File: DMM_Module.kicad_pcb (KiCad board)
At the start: 2 copper layers, 60 x 96 mm, 11 parts, among them J1 M20-7810245, J2 M20-7810245, J3 M20-7810245, J4 M20-7810245, J5 M20-7812045, J6 M20-7812045

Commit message: preliminary placement
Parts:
- added C1: 5p, Capacitor_SMD:C_0603_1608Metric, F.Cu at (74.3, 97.4)
- added C10: 1u, Capacitor_SMD:C_0603_1608Metric, F.Cu at (76.1, 114.8)
- added C11: 100n, Capacitor_SMD:C_0603_1608Metric, F.Cu at (71.3, 103.2)
- added C12: 10u, Capacitor_SMD:C_0603_1608Metric, F.Cu at (85.9, 111.0)
- added C13: 100n, Capacitor_SMD:C_0603_1608Metric, F.Cu at (88.7, 101.4)
- added C14: 1u, Capacitor_SMD:C_0603_1608Metric, F.Cu at (100.3, 101.6)
- added C15: 100n, Capacitor_SMD:C_0603_1608Metric, F.Cu at (92.3, 100.6)
- added C16: 2u2, Capacitor_SMD:C_0603_1608Metric, F.Cu at (93.1, 102.8)
- added C17: 1u, Capacitor_SMD:C_0603_1608Metric, F.Cu at (93.1, 105.8)
- added C18: 100n, Capacitor_SMD:C_0603_1608Metric, F.Cu at (88.5, 131.0)
- added C2: 10n, Capacitor_SMD:C_0603_1608Metric, F.Cu at (77.9, 94.6)
- added C3: 5p, Capacitor_SMD:C_0603_1608Metric, F.Cu at (85.1, 97.4)
- added C4: 1u, Capacitor_SMD:C_0603_1608Metric, F.Cu at (72.5, 112.0)
- added C5: 10u, Capacitor_SMD:C_0603_1608Metric, F.Cu at (71.3, 105.6)
- added C6: 27n, Capacitor_SMD:C_0603_1608Metric, F.Cu at (84.5, 114.8)
- added C7: 18p, Capacitor_SMD:C_0603_1608Metric, F.Cu at (93.5, 117.0)
- added C8: 18p, Capacitor_SMD:C_0603_1608Metric, F.Cu at (93.5, 110.6)
- added C9: 100n, Capacitor_SMD:C_0603_1608Metric, F.Cu at (74.9, 114.8)
- added D1: 1.2V, Package_TO_SOT_SMD:SOT-23-3, F.Cu at (70.3, 118.4)
- added D2: SX33L, Diode_SMD:D_SOD-123, F.Cu at (84.5, 142.0)
- added D3: SX33L, Diode_SMD:D_SOD-123, F.Cu at (107.1, 138.6)
- added D4: SX33L, Diode_SMD:D_SOD-123, F.Cu at (107.1, 135.2)
- added D5: SX33L, Diode_SMD:D_SOD-123, F.Cu at (107.1, 131.8)
- added D6: VRC_I, LED_SMD:LED_0603_1608Metric, B.Cu at (61.3, 140.6)
- added D7: 2W_4W, LED_SMD:LED_0603_1608Metric, B.Cu at (61.3, 136.6)
- added D8: uA_mA, LED_SMD:LED_0603_1608Metric, B.Cu at (61.3, 132.6)
- added D9: umA_A, LED_SMD:LED_0603_1608Metric, B.Cu at (61.3, 128.6)
- added K1: G6K-2F-Y-TR, sesa:DPDT_G6K-2F-Y, F.Cu at (67.4, 67.1)
- added K2: G6K-2F-Y-TR, sesa:DPDT_G6K-2F-Y, F.Cu at (100.2, 67.0)
- added K3: G6K-2F-Y-TR, sesa:DPDT_G6K-2F-Y, F.Cu at (100.2, 91.0)
- added K4: G6K-2F-Y-TR, sesa:DPDT_G6K-2F-Y, F.Cu at (100.2, 79.0)
- added L1: 1k@100MHz, Inductor_SMD:L_0603_1608Metric, F.Cu at (93.1, 104.4)
- added NT1: NetTie_4, NetTie:NetTie-4_SMD_Pad2.0mm, F.Cu at (97.9, 106.4)
- added Q1: DMN2056U, Package_TO_SOT_SMD:SOT-23, F.Cu at (84.1, 139.0)
- added Q2: DMN2056U, Package_TO_SOT_SMD:SOT-23, F.Cu at (102.3, 138.6)
- added Q3: DMN2056U, Package_TO_SOT_SMD:SOT-23, F.Cu at (102.3, 135.2)
- added Q4: DMN2056U, Package_TO_SOT_SMD:SOT-23, F.Cu at (102.3, 131.8)
- added R1: 10M, Resistor_SMD:R_0603_1608Metric, F.Cu at (74.3, 94.6)
- added R10: 10M, Resistor_SMD:R_0603_1608Metric, F.Cu at (83.9, 97.4)
- added R11: 30k, Resistor_SMD:R_0603_1608Metric, F.Cu at (85.1, 94.6)
- added R12: 100, Resistor_SMD:R_0603_1608Metric, F.Cu at (70.7, 96.8)
- added R13: 1k5, Resistor_SMD:R_0805_2012Metric, F.Cu at (70.7, 93.8)
- added R14: 910k, Resistor_SMD:R_0603_1608Metric, F.Cu at (78.5, 114.8)
- added R15: 100k, Resistor_SMD:R_0603_1608Metric, F.Cu at (79.7, 114.8)
- added R16: 10k, Resistor_SMD:R_0603_1608Metric, F.Cu at (71.3, 109.2)
- added R17: 10k, Resistor_SMD:R_0603_1608Metric, F.Cu at (77.3, 114.8)
- added R18: 10k, Resistor_SMD:R_0603_1608Metric, F.Cu at (71.3, 110.4)
- added R19: 1M, Resistor_SMD:R_0603_1608Metric, F.Cu at (71.3, 108.0)
- added R2: 1k, Resistor_SMD:R_0603_1608Metric, F.Cu at (75.5, 94.6)
- added R20: 10k, Resistor_SMD:R_0603_1608Metric, F.Cu at (71.3, 106.8)
- added R21: 10k, Resistor_SMD:R_0603_1608Metric, F.Cu at (69.3, 114.8)
- added R22: 10k, Resistor_SMD:R_0603_1608Metric, F.Cu at (71.3, 104.4)
- added R23: 91k, Resistor_SMD:R_0603_1608Metric, F.Cu at (81.3, 114.8)
- added R24: 91k, Resistor_SMD:R_0603_1608Metric, F.Cu at (82.9, 114.8)
- added R25: 10k, Resistor_SMD:R_0603_1608Metric, F.Cu at (82.9, 117.6)
- added R26: 10k, Resistor_SMD:R_0603_1608Metric, F.Cu at (81.3, 117.6)
- added R27: 10m, Resistor_SMD:R_0805_2012Metric, F.Cu at (84.3, 74.0)
- added R28: 910, Resistor_SMD:R_0805_2012Metric, F.Cu at (84.3, 77.4)
- added R29: 80m, Resistor_SMD:R_0805_2012Metric, F.Cu at (84.3, 80.8)
- added R3: 10M, Resistor_SMD:R_0603_1608Metric, F.Cu at (76.7, 94.6)
- added R30: 24, Resistor_SMD:R_0805_2012Metric, F.Cu at (84.3, 87.6)
- added R31: 75, Resistor_SMD:R_0805_2012Metric, F.Cu at (84.3, 84.2)
- added R32: 33, Resistor_SMD:R_0603_1608Metric, F.Cu at (88.7, 105.6)
- added R33: 1M, Resistor_SMD:R_0603_1608Metric, F.Cu at (88.7, 103.2)
- added R34: 1M, Resistor_SMD:R_0603_1608Metric, F.Cu at (88.7, 104.4)
- added R35: 1M, Resistor_SMD:R_0603_1608Metric, F.Cu at (93.5, 113.8)
- added R38: 11k, Resistor_SMD:R_0603_1608Metric, F.Cu at (93.1, 98.0)
- added R39: 21k, Resistor_SMD:R_0603_1608Metric, F.Cu at (93.9, 100.6)
- added R4: 1k, Resistor_SMD:R_0603_1608Metric, F.Cu at (79.1, 94.6)
- added R41: 10k, Resistor_SMD:R_0603_1608Metric, F.Cu at (86.7, 139.0)
- added R42: 10k, Resistor_SMD:R_0603_1608Metric, F.Cu at (99.7, 138.4)
- added R43: 10k, Resistor_SMD:R_0603_1608Metric, F.Cu at (99.7, 135.2)
- added R44: 10k, Resistor_SMD:R_0603_1608Metric, F.Cu at (99.7, 131.8)
- added R45: 10k, Resistor_SMD:R_0603_1608Metric, F.Cu at (90.7, 129.4)
- added R46: 10k, Resistor_SMD:R_0603_1608Metric, F.Cu at (90.7, 128.2)
- added R5: 10k, Resistor_SMD:R_0603_1608Metric, F.Cu at (80.3, 94.6)
- added R6: 1k, Resistor_SMD:R_0603_1608Metric, F.Cu at (81.5, 97.4)
- added R7: 100k, Resistor_SMD:R_0603_1608Metric, F.Cu at (81.5, 94.6)
- added R8: 1M, Resistor_SMD:R_0603_1608Metric, F.Cu at (82.7, 94.6)
- added R9: 110k, Resistor_SMD:R_0603_1608Metric, F.Cu at (82.7, 97.4)
- added RN1: 33, Resistor_SMD:R_Array_Convex_4x0603, F.Cu at (91.9, 138.8)
- added RN2: 1k, Resistor_SMD:R_Array_Convex_4x0603, F.Cu at (88.1, 133.8)
- added U1: HY3131, Package_QFP:LQFP-48_7x7mm_P0.5mm, F.Cu at (80.3, 106.0)
- added U2: TPS7A2401DBVR, Package_TO_SOT_SMD:SOT-23-5, F.Cu at (97.3, 101.4)
- added U3: PI4IOE5V9536UEX, Package_SO:TSSOP-8_3x3mm_P0.65mm, F.Cu at (91.9, 133.2)
- added X1: 4.9152MHz, Crystal:Crystal_SMD_HC49-SD, F.Cu at (89.7, 113.8)
- J1, J2: footprint bynet_Connectors:Header_SKT_02x02_Fixed_Harwin_M20-7810245 -> bynet:Header_SKT_02x02_Fixed_Harwin_M20-7810245
- J3, J4: value M20-7810245 -> M20-7812045; footprint bynet_Connectors:Header_SKT_02x02_Fixed_Harwin_M20-7810245 -> bynet:Header_SKT_02x20_Fixed_Harwin_M20-7812045
- J5, J6: value M20-7812045 -> M20-7810245; footprint bynet_Connectors:Header_SKT_02x20_Fixed_Harwin_M20-7812045 -> bynet:Header_SKT_02x02_Fixed_Harwin_M20-7810245
- moved J4 50.8 mm to (60.2, 86.1), turned to 90 degrees
- moved J6 50.8 mm to (100.8, 55.6), turned to -90 degrees
- moved J3 35.3 mm to (108.5, 86.1)
- moved J5 35.3 mm to (90.7, 55.6)
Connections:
- net /N renamed GNDA
- net /P renamed /DMM_IN
- J3 pad 1: /SN -> 12V
- J3 pad 2: /SN -> 5V
- J3 pad 3: /SN -> unconnected-(J3-RF0-Pad3)
- J3 pad 4: /SN -> unconnected-(J3-RF4-Pad4)
- J4 pad 1: /SP -> 12V
- J4 pad 2: /SP -> 5V
- J4 pad 3: /SP -> unconnected-(J4-RF0-Pad3)
- J4 pad 4: /SP -> unconnected-(J4-RF4-Pad4)
- J5 pad 1: +12V -> /FourWireRet
- J5 pad 2: +5V -> /FourWireRet
- J5 pad 3: unconnected-(J5-RF0-Pad3) -> /FourWireRet
- J5 pad 4: unconnected-(J5-RF4-Pad4) -> /FourWireRet
- J6 pad 1: +12V -> /FourWireCurr
- J6 pad 2: +5V -> /FourWireCurr
- J6 pad 3: unconnected-(J6-RB0-Pad3) -> /FourWireCurr
- J6 pad 4: unconnected-(J6-RB4-Pad4) -> /FourWireCurr

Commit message: Board is fully routed
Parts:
- D1: footprint Package_TO_SOT_SMD:SOT-23-3 -> Package_TO_SOT_SMD:SOT-23
- D6, D7, D8, D9: moved to F.Cu
- R28: value 910 -> 910m
- moved D6 91.6 mm to (151.3, 123.6)
- moved D7 91.6 mm to (151.3, 119.6)
- moved D8 91.6 mm to (151.3, 115.6)
- moved D9 91.6 mm to (151.3, 111.6)
- moved X1 86.7 mm to (174.7, 96.8)
- moved C13 86.4 mm to (172.7, 81.0)
- moved R12 85.9 mm to (155.0, 80.3)
- moved R13 85.9 mm to (155.0, 77.3), turned to -90 degrees
- moved K2 85.7 mm to (184.2, 50.0)
- moved K3 85.7 mm to (184.2, 74.0)
- moved K4 85.7 mm to (184.2, 62.0)
- moved D1 85.7 mm to (154.2, 101.4)
- moved R21 85.7 mm to (153.2, 97.8)
- moved C12 84.7 mm to (168.9, 94.0)
- moved C18 84.7 mm to (171.5, 114.0)
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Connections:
- net Net-(D2-A) renamed /Power/RELAY0
- net Net-(D3-A) renamed /Power/RELAY1
- net Net-(D4-A) renamed /Power/RELAY2
- net Net-(D5-A) renamed /Power/RELAY3
- J3 pad 1: 12V -> unconnected-(J3-+12V-Pad1)
- J4 pad 1: 12V -> unconnected-(J4-+12V-Pad1)
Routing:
- net /DMM DAQ/VdOhmCap: track 0.00 -> 107.4 mm, vias 0 -> 5
- net /Power/RELAY1: track 0.00 -> 83.1 mm, vias 0 -> 2
- net /Power/RELAY0: track 0.00 -> 83.0 mm, vias 0 -> 2
- net /Power/RELAY3: track 0.00 -> 69.5 mm, vias 0 -> 2
- net /SCL: track 0.00 -> 66.5 mm, vias 0 -> 2
- net VDD: track 0.00 -> 65.5 mm, vias 0 -> 3
- net /SDA: track 0.00 -> 63.1 mm, vias 0 -> 2
- net /~{CS}: track 0.00 -> 54.1 mm, vias 0 -> 2
- net /Power/RELAY2: track 0.00 -> 53.0 mm, vias 0 -> 2
- net Net-(K2B-COM2): track 0.00 -> 51.2 mm, vias 0 -> 2
- net /DMM DAQ/I_uAmp: track 0.00 -> 47.1 mm, vias 0 -> 2
- net /SCLK: track 0.00 -> 46.0 mm, vias 0 -> 2
- net /MOSI: track 0.00 -> 45.4 mm, vias 0 -> 2
- net /MISO: track 0.00 -> 43.1 mm, vias 0 -> 2
- net Net-(K2A-COM1): track 0.00 -> 40.7 mm, vias 0 -> 2
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- added copper zone on In2.Cu, net 5V
- added copper zone on B.Cu, net GND
- added copper zone on F.Cu, net GND
- added copper zone on In1.Cu, net GND
- added copper zone on F.Cu, net GNDA
- added copper zone on F.Cu, net VSSA
- added copper zone on In1.Cu, net VSSA
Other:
- copper layers 2 -> 4
- board text added: "2W_4W"
- board text added: "DMM_COM"
- board text added: "DMM_IN"
- board text added: "FourWireCurr"
- board text added: "FourWireRet"
- board text added: "VRC_I"
- board text added: "uA_mA"
- board text added: "umA_A"

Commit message: Step and gerber files added
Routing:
- net GNDA: track 1.47 -> 0.00 mm
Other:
- board text added: "0"
- board text added: "0 mm"
- board text added: "0.01 mm"
- board text added: "0.02"
- board text added: "0.035 mm"
- board text added: "0.1900 mm"
- board text added: "0.2000 mm"
- board text added: "0.2000 mm / 0.2000 mm"
- board text added: "1"
- board text added: "3.3"
- board text added: "4"
- board text added: "4.5"
- board text added: "60.0010 mm x 96.0010 mm"
- board text added: "B.Cu"
- board text added: "B.Mask"
- board text added: "B.Paste"
- board text added: "B.Silkscreen"
- board text added: "BOARD CHARACTERISTICS"
- board text added: "Black"
- board text added: "Board Thickness:"
- board text added: "Board overall dimensions:"
- board text added: "Bottom Silk Screen"
- board text added: "Bottom Solder Mask"
- board text added: "Bottom Solder Paste"
- board text added: "Castellated pads:"
- board text added: "Color"
- board text added: "Copper Finish:"
- board text added: "Copper Layer Count:"
- board text added: "Dielectric 1"
- board text added: "Dielectric 2"
- board text added: "Dielectric 3"
- board text added: "ENIG"
- board text added: "Edge card connectors:"
- board text added: "Epsilon R"
- board text added: "F.Cu"
- board text added: "F.Mask"
- board text added: "F.Paste"
- board text added: "F.Silkscreen"
- board text added: "FR4"
- board text added: "Impedance Control:"
- board text added: "Layer Name"
- board text added: "Loss Tangent"
- board text added: "Material"
- board text added: "Min hole diameter:"
- board text added: "Min track/spacing:"
- board text added: "No"
- board text added: "Not specified"
- board text added: "Plated Board Edge:"
- board text added: "Power"
- board text added: "Signal"
- board text added: "Thickness (mm)"
- board text added: "Top Silk Screen"
- board text added: "Top Solder Mask"
- board text added: "Top Solder Paste"
- board text added: "Type"
- board text added: "White"
- board text added: "copper"
- board text added: "core"
- board text added: "prepreg"

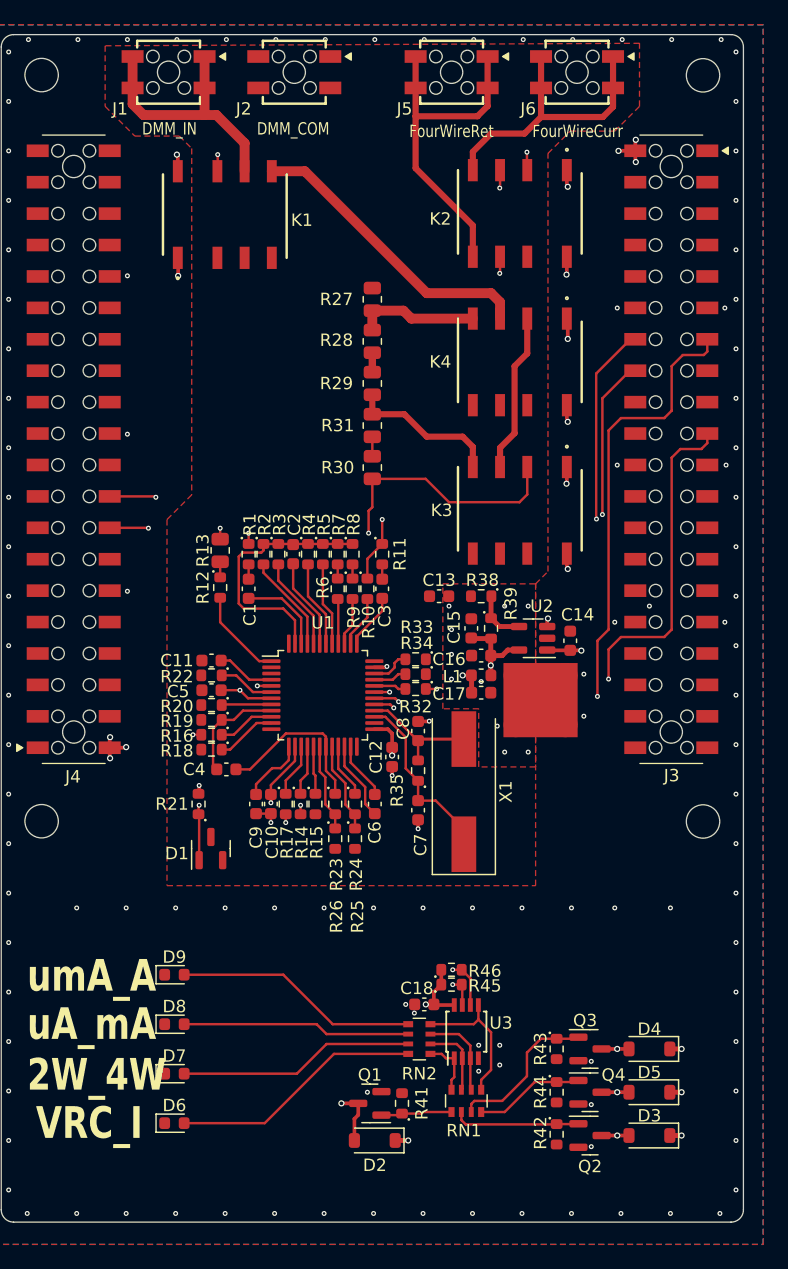
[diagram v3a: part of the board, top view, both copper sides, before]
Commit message: Added galvanic isolation
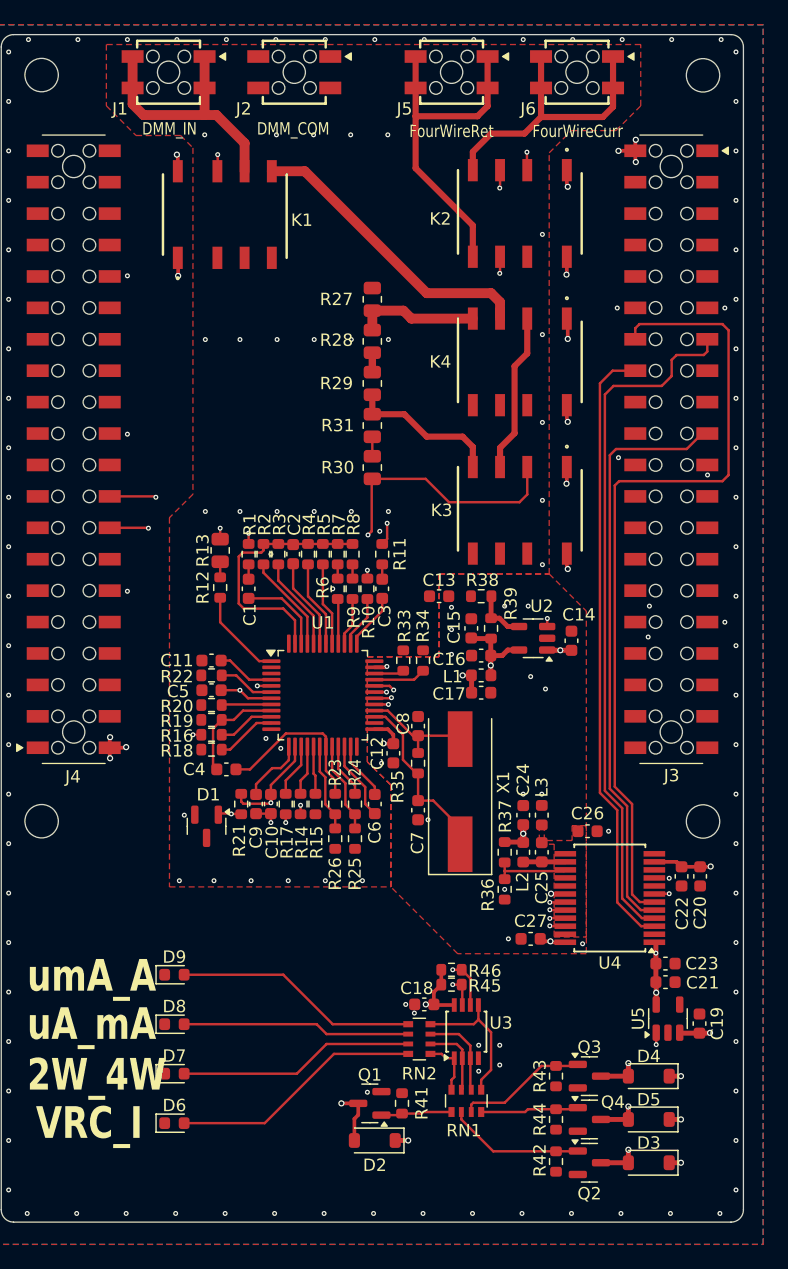
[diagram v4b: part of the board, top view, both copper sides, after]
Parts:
- removed NT1: NetTie_4, NetTie:NetTie-4_SMD_Pad2.0mm
- removed R32: 33, Resistor_SMD:R_0603_1608Metric
- added C19: 2u2, Capacitor_SMD:C_0603_1608Metric, F.Cu at (193.7, 115.5)
- added C20: 10u, Capacitor_SMD:C_0603_1608Metric, F.Cu at (193.8, 103.6)
- added C21: 2u2, Capacitor_SMD:C_0603_1608Metric, F.Cu at (191.0, 112.2)
- added C22: 100n, Capacitor_SMD:C_0603_1608Metric, F.Cu at (192.3, 103.6)
- added C23: 100n, Capacitor_SMD:C_0603_1608Metric, F.Cu at (191.0, 110.7)
- added C24: 10u, Capacitor_SMD:C_0603_1608Metric, F.Cu at (179.5, 98.7)
- added C25: 100n, Capacitor_SMD:C_0603_1608Metric, F.Cu at (181.0, 101.7)
- added C26: 100p, Capacitor_SMD:C_0603_1608Metric, F.Cu at (184.7, 100.0)
- added C27: 100n, Capacitor_SMD:C_0603_1608Metric, F.Cu at (180.1, 108.7)
- added L2: 1k@100MHz, Inductor_SMD:L_0603_1608Metric, F.Cu at (179.5, 101.7)
- added L3: 1k@100MHz, Inductor_SMD:L_0603_1608Metric, F.Cu at (181.0, 98.7)
- added R36: 10k, Resistor_SMD:R_0603_1608Metric, F.Cu at (178.0, 104.7)
- added R37: 30k, Resistor_SMD:R_0603_1608Metric, F.Cu at (178.0, 101.7)
- added U4: ADUM5411BRSZ, Package_SO:SSOP-24_5.3x8.2mm_P0.65mm, F.Cu at (186.5, 105.4)
- added U5: NCP164CSN330T1G, Package_TO_SOT_SMD:SOT-23-5, F.Cu at (191.2, 115.1)
- C1, C3: value 5p -> 5p1
- G***: footprint bynet_Logos:BYNET_LOGO_1200x1200 -> bynet:BYNET_LOGO_1200x1200
- RN2: value 1k -> 4k7
- moved R21 3.45 mm to (156.7, 97.8)
- moved Q2 2.20 mm to (184.8, 126.8)
- moved Q3 2.20 mm to (184.8, 119.8)
- moved Q4 2.20 mm to (184.8, 123.3)
- moved D3 2.20 mm to (189.6, 126.8)
- moved D4 2.20 mm to (189.6, 119.8)
- moved D5 2.20 mm to (189.6, 123.3)
- moved R42 2.20 mm to (182.1, 126.7)
- moved R43 2.20 mm to (182.1, 119.8)
- moved R44 2.20 mm to (182.1, 123.3)
- moved D1 1.83 mm to (153.9, 99.6), turned to -90 degrees
- moved R34 1.25 mm to (171.4, 86.2), turned to -90 degrees
- moved R33 1.00 mm to (169.8, 86.2), turned to -90 degrees
- moved R35 0.60 mm to (171.0, 94.5)
- moved C8 0.40 mm to (171.0, 91.5)
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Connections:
- C12 pad 1: GND -> VSSA
- C14 pad 1: GND -> VSSA
- C14 pad 2: 5V -> /5V_ISO
- C18 pad 2: VDD -> 3V3
- C7 pad 1: GND -> VSSA
- C8 pad 1: GND -> VSSA
- J3 pad 13: /~{CS} -> /Interface/~{CS}_SYS
- J3 pad 14: /MISO -> /Interface/MISO_SYS
- J3 pad 16: /MOSI -> /Interface/MOSI_SYS
- J3 pad 19: /SCLK -> /Interface/SCLK_SYS
- K1 pad 1: /Power/RELAY0 -> 5V
- K1 pad 8: 5V -> /Power/RELAY0
- K2 pad 1: /Power/RELAY1 -> 5V
- K2 pad 8: 5V -> /Power/RELAY1
- K3 pad 1: /Power/RELAY2 -> 5V
- K3 pad 8: 5V -> /Power/RELAY2
- K4 pad 1: /Power/RELAY3 -> 5V
- K4 pad 8: 5V -> /Power/RELAY3
- R45 pad 1: VDD -> 3V3
- R46 pad 1: VDD -> 3V3
- U1 pad 32: Net-(U1B-DO) -> /MISO
- U1 pad 35: GND -> VSSA
- U2 pad 1: 5V -> /5V_ISO
- U2 pad 2: GND -> VSSA
- U2 pad 3: 5V -> /5V_ISO
- U3 pad 8: VDD -> 3V3
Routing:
- net /Interface/MISO_SYS: track 0.00 -> 65.7 mm
- net /Interface/~{CS}_SYS: track 0.00 -> 56.0 mm
- net /Interface/MOSI_SYS: track 0.00 -> 49.6 mm
- net /Interface/SCLK_SYS: track 0.00 -> 47.5 mm
- net 3V3: track 0.00 -> 36.1 mm, vias 0 -> 4
- net /5V_ISO: track 0.00 -> 24.7 mm, vias 0 -> 4
- net /~{CS}: track 54.1 -> 30.2 mm
- net /Power/RELAY0: track 83.0 -> 98.9 mm
- net /SCLK: track 46.0 -> 30.5 mm
- net /MOSI: track 45.4 -> 31.8 mm
- net /MISO: track 43.1 -> 31.0 mm
- net VDD: track 65.0 -> 54.9 mm, vias 3 -> 4
- net /Power/RELAY3: track 69.5 -> 62.9 mm
- net Net-(U4-Vsel): track 0.00 -> 6.30 mm
- net /Power/RELAY2: track 53.0 -> 47.0 mm
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- added copper zone on F.Cu, net /Interface/GNDiso
- added copper zone on In1.Cu, net GNDA
- added copper zone on In2.Cu, net GNDA
- added copper zone on In2.Cu, net VSSA

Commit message: Board thickness adjusted
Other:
- board text added: "0.1 mm"
- board text added: "1.24 mm"
